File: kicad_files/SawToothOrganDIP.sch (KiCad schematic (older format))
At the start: 31 parts, among them J1 Conn_01x01, J2 Conn_01x01, J3 Conn_01x01, Q1 Q_NPN_CBE, Q2 Q_NPN_CBE, Q3 Q_NPN_CBE, Q4 Q_PNP_CBE, SW1 SW_DIP_x01, U1 Keyboard

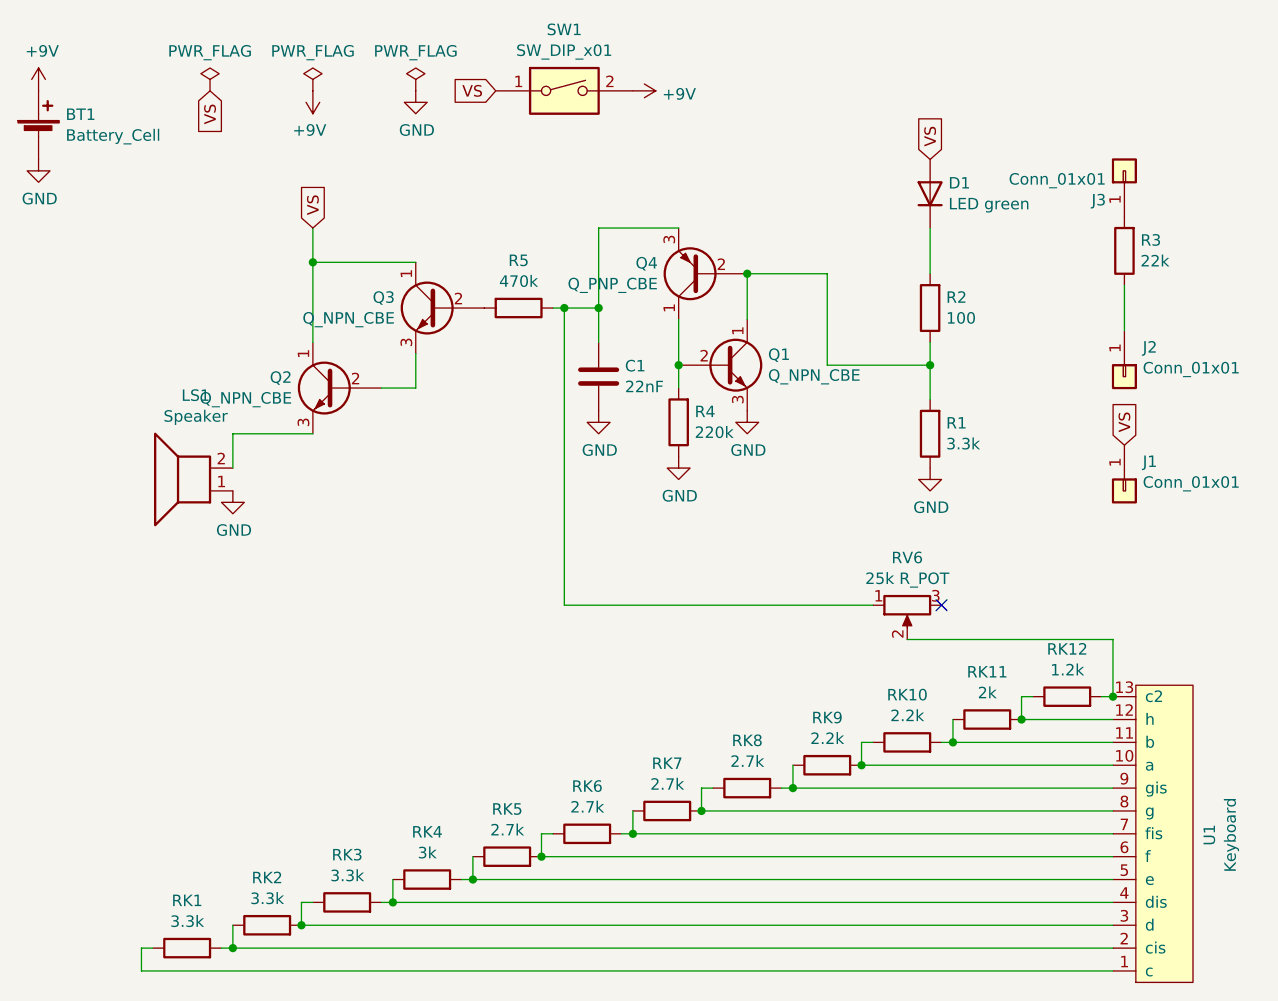
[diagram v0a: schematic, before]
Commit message: added gerber-files and another resistor
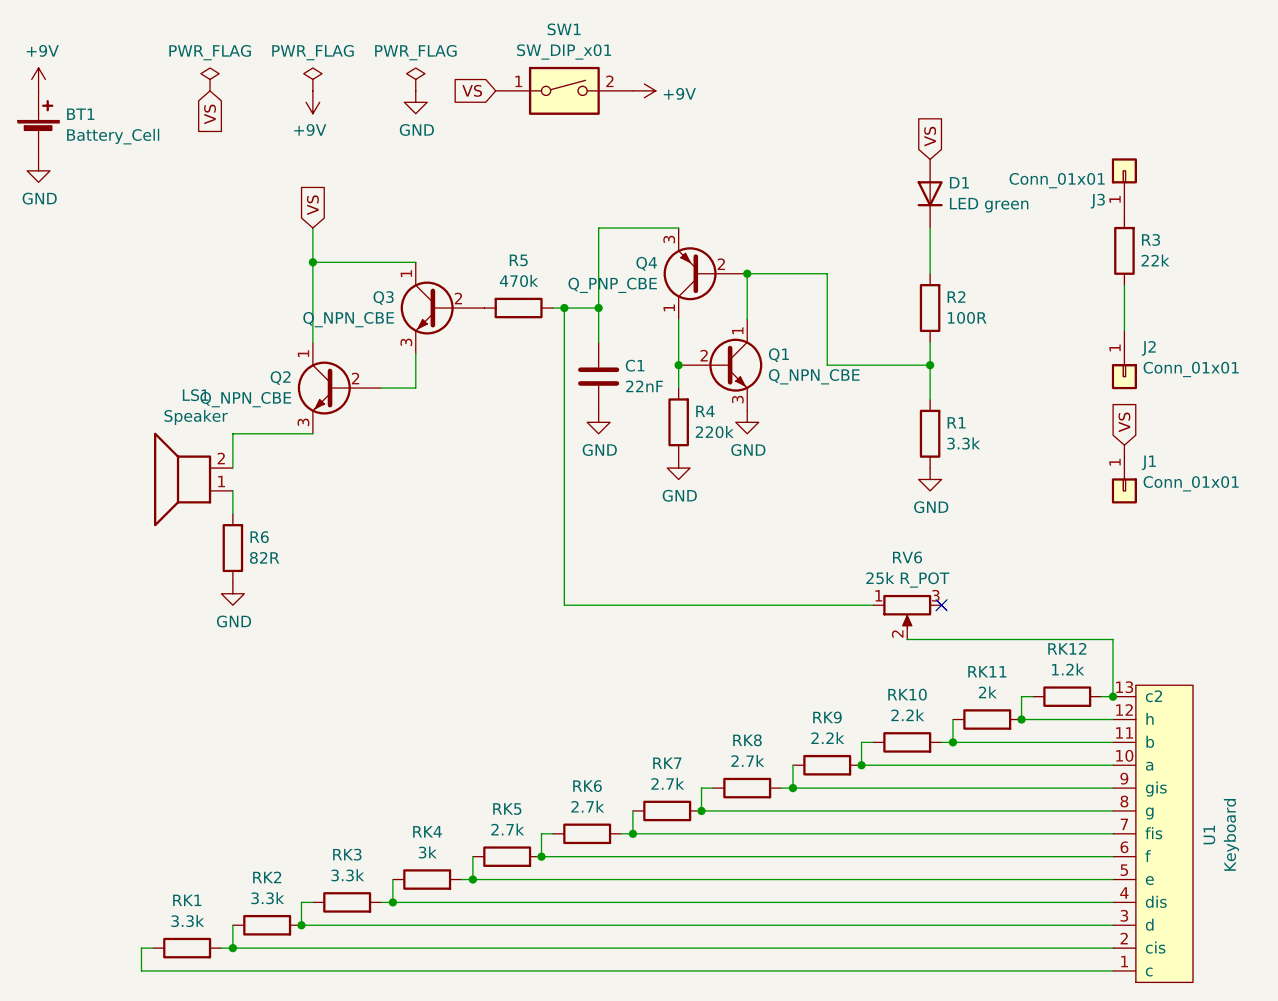
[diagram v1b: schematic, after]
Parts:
- added R6: 82R, Resistor_THT:R_Axial_DIN0207_L6.3mm_D2.5mm_P10.16mm_Horizontal, symbol Device:R
- R2: value 100 -> 100R
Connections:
- net GND: now also R6.1; no longer LS1.1
- new net: LS1.1, R6.2
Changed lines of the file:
@@
 L power:GND #PWR0106
 U 1 1 5F67C5BD
-P 1600 2600
-F 0 "#PWR0106" H 1600 2350 50  0001 C CNN
-F 1 "GND" H 1605 2427 50  0000 C CNN
-F 2 "" H 1600 2600 50  0001 C CNN
-F 3 "" H 1600 2600 50  0001 C CNN
-	1    1600 2600
+P 1600 3000
+F 0 "#PWR0106" H 1600 2750 50  0001 C CNN
+F 1 "GND" H 1605 2827 50  0000 C CNN
+F 2 "" H 1600 3000 50  0001 C CNN
+F 3 "" H 1600 3000 50  0001 C CNN
+	1    1600 3000
 	1    0    0    -1
 $EndComp
@@
 P 4650 1800
 F 0 "R2" H 4580 1754 50  0000 R CNN
-F 1 "100" H 4580 1845 50  0000 R CNN
+F 1 "100R" H 4580 1845 50  0000 R CNN
 F 2 "Resistor_THT:R_Axial_DIN0207_L6.3mm_D2.5mm_P10.16mm_Horizontal" V 4580 1800 50  0001 C CNN
 F 3 "~" H 4650 1800 50  0001 C CNN
@@
 	0    -1   -1   0
 $EndComp
+$Comp
+L Device:R R6
+U 1 1 5F82240C
+P 1600 2850
+F 0 "R6" H 1530 2804 50  0000 R CNN
+F 1 "82R" H 1530 2895 50  0000 R CNN
+F 2 "Resistor_THT:R_Axial_DIN0207_L6.3mm_D2.5mm_P10.16mm_Horizontal" V 1530 2850 50  0001 C CNN
+F 3 "~" H 1600 2850 50  0001 C CNN
+	1    1600 2850
+	-1   0    0    1
+$EndComp
+Wire Wire Line
+	1600 2600 1600 2700
 $EndSCHEMATC
